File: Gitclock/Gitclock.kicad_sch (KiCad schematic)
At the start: 41 parts, among them J1 PJ-102AH, J2 Conn_01x06, SW1 Omron_B3F_SPST, SW5 RotaryEncoder_Switch, U1 ATmega328-PU, U2 L7805, U3 MAX7219, U4 DS1307_DIP-8, Y1 Crystal_16MHz, Y2 Crystal_32768Hz

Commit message: CuckcooTicTocFINALCLOCK
Last Upload onto Github
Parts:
- removed C9: C_0805_0.1uf, footprints:C_0805_2012Metric, symbol HPS:C_0805_0.1uf
- removed R12: R_0805_10K, footprints:R_0805_2012Metric, symbol HPS:R_0805_10K
- removed RV1: R_POT_10K, footprints:Potentiometer_Bourns_3386P_Vertical, symbol HPS:R_POT_10K
- added C9: C_0805_10uf, footprints:C_0805_2012Metric, symbol HPS:C_0805_10uf
- added J3: Conn_02x03_Odd_Even, footprints:PinHeader_2x03_P2.54mm_Vertical, symbol HPS:Conn_02x03_Odd_Even
- added Q1: NPN_2N3904_SOT23, footprints:SOT-23, symbol HPS:NPN_2N3904_SOT23
- added R11: R_0805_2.2K, footprints:R_0805_2012Metric, symbol HPS:R_0805_2.2K
- added R12: R_0805_22K, footprints:R_0805_2012Metric, symbol HPS:R_0805_22K
- added R5: R_0805_1K, footprints:R_0805_2012Metric, symbol HPS:R_0805_1K
- added TP1, TP2, TP3, TP4, TP5: TestPoint, footprints:TestPoint_THTPad_D2.0mm_Drill1.0mm, symbol HPS:TestPoint
- SW5: Digikey PN 987-1398-ND -> 987-1188-ND
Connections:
- net BUZZER: now also R11.1; no longer BZ1.2 (+)
- net CLK: now also TP4.1
- net DATA: now also TP2.1
- net GND: now also D1.1 (K), C9.2, J3.6 (Pin_6), Q1.2 (E), TP3.1; no longer BZ1.1 (-), R1.2
- net LED_SCK: now also R1.1, J3.3 (Pin_3); no longer D1.2 (A)
- net LOAD: now also TP1.1
- net MOSI: now also J3.4 (Pin_4)
- net RESET: now also J3.5 (Pin_5)
- net RS: now also J3.1 (Pin_1)
- net VCC: now also BZ1.1 (-), C9.1, J3.2 (Pin_2), R12.1, R5.1, TP5.1
- net at U3.18 (ISET): now also R12.2
- net Select_B: no longer names the net of U1.25 (ADC2/PC2)
- new net: Q1.1 (B), R11.2
- new net: BZ1.2 (+), Q1.3 (C), R5.2
- new net: D1.2 (A), R1.2
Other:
- moved on the sheet: BZ1, D1, R1

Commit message: changed pull down to pull up and swapped RX and TX connection
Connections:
- net GND: no longer R10.2, R6.2, R7.2
- net MENU OUTPUT2: now also R7.2; no longer R7.1
- net MENU SCROLL: now also R6.2; no longer R6.1
- net MENU_B: now also R10.2; no longer R10.1
- net RXD: now also R3.1; no longer R4.1
- net TXD: now also R4.1; no longer R3.1
- net VCC: now also R10.1, R6.1, R7.1
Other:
- moved on the sheet: R10, R6, R7

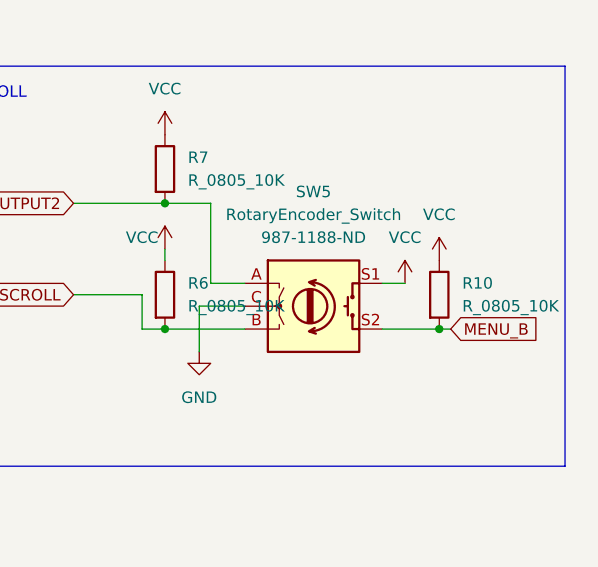
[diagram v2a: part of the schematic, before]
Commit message: Changed Encoder connection on SW from VCC to GND
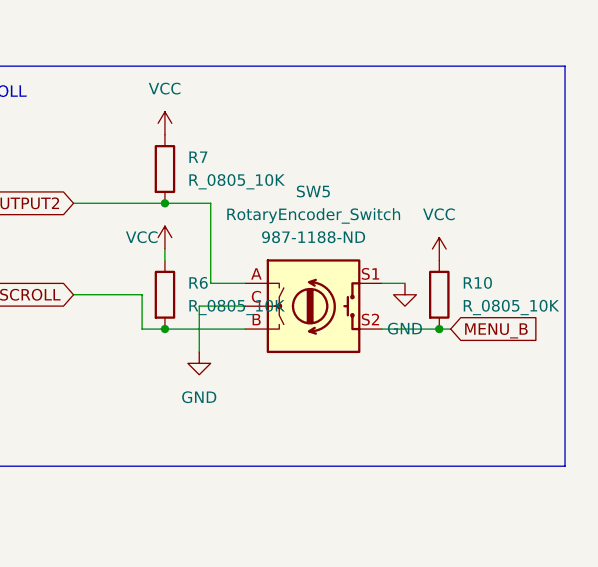
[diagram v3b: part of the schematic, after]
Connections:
- net GND: now also SW5.S1
- net VCC: no longer SW5.S1
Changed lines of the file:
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@@
     (pin "6")
-  )
-  (symbol (lib_id "HPS:VCC") (at 384.81 63.5 0) (unit 1)
-    (in_bom yes) (on_board yes) (fields_autoplaced)
-    (property "Reference" "#PWR019" (id 0) (at 384.81 67.31 0)
-      (effects (font (size 1.27 1.27)) hide)
-    )
-    (property "Value" "VCC" (id 1) (at 384.81 58.42 0))
-    (property "Footprint" "" (id 2) (at 384.81 63.5 0)
-      (effects (font (size 1.27 1.27)) hide)
-    )
-    (property "Datasheet" "" (id 3) (at 384.81 63.5 0)
-      (effects (font (size 1.27 1.27)) hide)
-    )
-    (pin "1")
   )
   (symbol (lib_id "HPS:R_0805_10K") (at 226.06 165.1 0) (unit 1)
@@
     (pin "1")
   )
+  (symbol (lib_id "HPS:GND") (at 384.81 63.5 0) (unit 1)
+    (in_bom yes) (on_board yes) (fields_autoplaced)
+    (property "Reference" "#PWR0104" (id 0) (at 384.81 69.85 0)
+      (effects (font (size 1.27 1.27)) hide)
+    )
+    (property "Value" "GND" (id 1) (at 384.81 68.58 0))
+    (property "Footprint" "" (id 2) (at 384.81 63.5 0)
+      (effects (font (size 1.27 1.27)) hide)
+    )
+    (property "Datasheet" "" (id 3) (at 384.81 63.5 0)
+      (effects (font (size 1.27 1.27)) hide)
+    )
+    (pin "1")
+  )
   (symbol (lib_id "HPS:PWR_FLAG") (at 60.96 114.3 0) (unit 1)
     (in_bom yes) (on_board yes) (fields_autoplaced)
@@
       (reference "#PWR018") (unit 1) (value "GND") (footprint "")
     )
-    (path "/3e0965fc-b789-493a-9f51-412a16a88e23"
-      (reference "#PWR019") (unit 1) (value "VCC") (footprint "")
-    )
     (path "/b3c36c95-a911-4edf-8a71-e8a00d2f2ff7"
       (reference "#PWR020") (unit 1) (value "VCC") (footprint "")
@@
       (reference "#PWR0103") (unit 1) (value "VCC") (footprint "")
     )
+    (path "/978809cd-641a-45f3-a18c-162b61bc0b0e"
+      (reference "#PWR0104") (unit 1) (value "GND") (footprint "")
+    )
     (path "/b625a70b-6b01-4ec2-b81a-d2af7627ba00"
